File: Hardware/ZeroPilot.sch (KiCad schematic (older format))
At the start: 5 parts

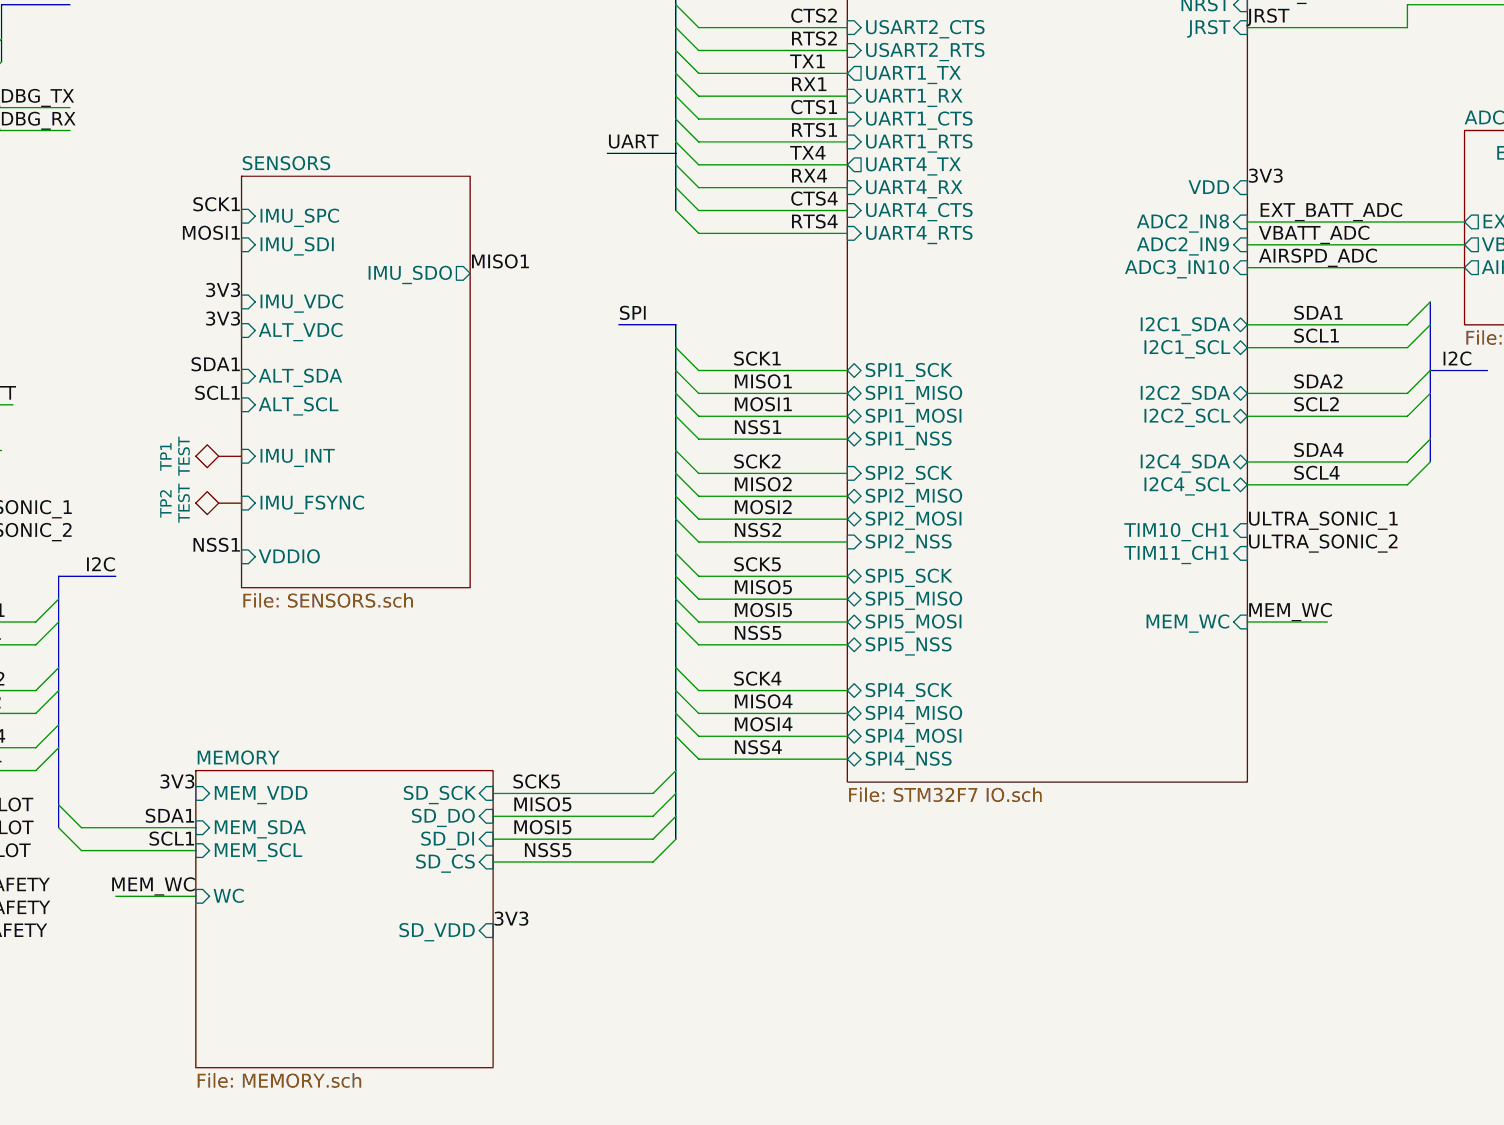
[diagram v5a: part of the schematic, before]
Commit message: Updated schematic
-Changed diode to 0603 diodes
-Changed SD card to proper pinout
-Fixed SPI1 conflict
-Renamed some power nets
-Fixed naming error in IMU NSS
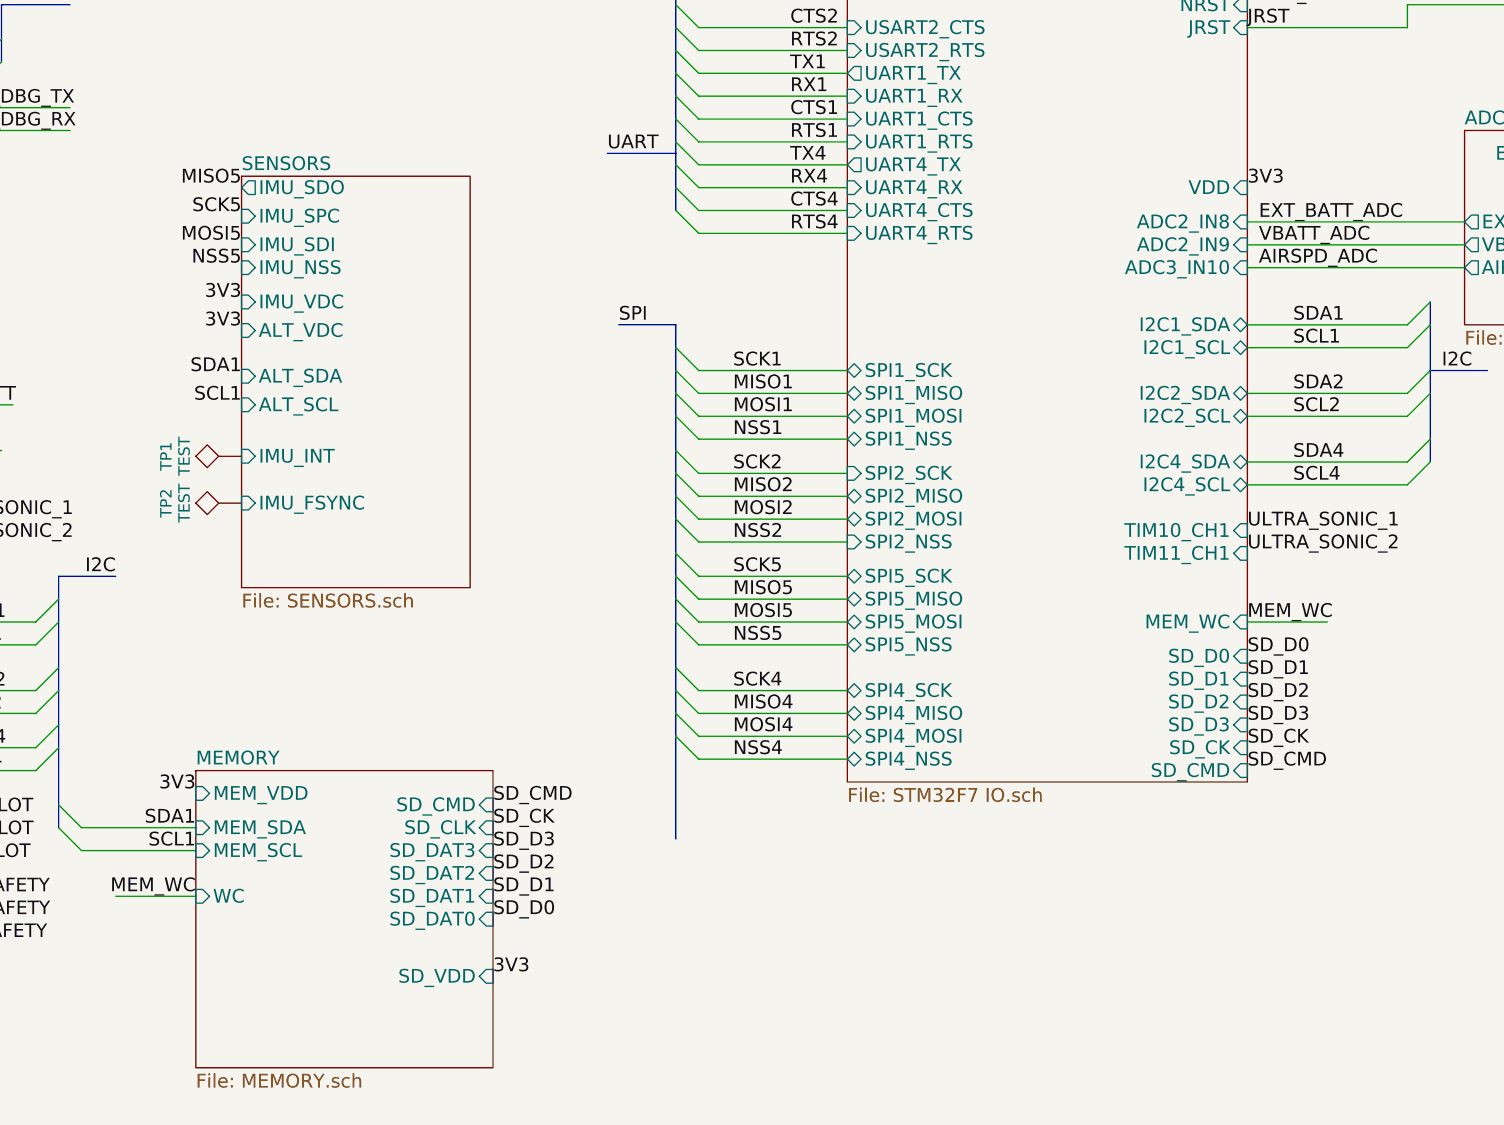
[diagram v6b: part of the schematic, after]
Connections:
- net labels added: SD_CK, SD_CMD, SD_D0, SD_D1, SD_D2, SD_D3
- wire segments 104 -> 100
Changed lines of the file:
@@
 F49 "SPI4_MOSI" B L 7200 6100 60
 F50 "MEM_WC" I R 8950 5600 60
+F51 "SD_D0" I R 8950 5750 60
+F52 "SD_D1" I R 8950 5850 60
+F53 "SD_D2" I R 8950 5950 60
+F54 "SD_D3" I R 8950 6050 60
+F55 "SD_CK" I R 8950 6150 60
+F56 "SD_CMD" I R 8950 6250 60
 $EndSheet
 Text Label 3550 850  2    60   ~ 0
@@
 F0 "MEMORY" 60
 F1 "MEMORY.sch" 60
-F2 "SD_DI" I R 5650 6550 60
-F3 "SD_DO" I R 5650 6450 60
-F4 "SD_SCK" I R 5650 6350 60
-F5 "SD_VDD" I R 5650 6950 60
-F6 "SD_CS" I R 5650 6650 60
-F7 "MEM_VDD" I L 4350 6350 60
-F8 "MEM_SDA" I L 4350 6500 60
-F9 "MEM_SCL" I L 4350 6600 60
-F10 "WC" I L 4350 6800 60
+F2 "SD_VDD" I R 5650 7150 60
+F3 "MEM_VDD" I L 4350 6350 60
+F4 "MEM_SDA" I L 4350 6500 60
+F5 "MEM_SCL" I L 4350 6600 60
+F6 "WC" I L 4350 6800 60
+F7 "SD_CMD" I R 5650 6400 60
+F8 "SD_DAT0" I R 5650 6900 60
+F9 "SD_CLK" I R 5650 6500 60
+F10 "SD_DAT3" I R 5650 6600 60
+F11 "SD_DAT1" I R 5650 6800 60
+F12 "SD_DAT2" I R 5650 6700 60
 $EndSheet
 Text Label 8950 5600 0    60   ~ 0
@@
 Text Label 4350 6350 2    60   ~ 0
 3V3
-Entry Wire Line
-	6450 6450 6350 6550
-Entry Wire Line
-	6450 6250 6350 6350
-Entry Wire Line
-	6450 6350 6350 6450
 Text Label 6200 4300 0    60   ~ 0
 SPI
@@
 NSS4
 Text Label 6700 5700 0    60   ~ 0
-NSS5
-Entry Wire Line
-	6450 6550 6350 6650
-Text Label 5950 6350 2    60   ~ 0
-SCK5
-Text Label 6000 6450 2    60   ~ 0
-MISO5
-Text Label 6000 6550 2    60   ~ 0
-MOSI5
-Text Label 6000 6650 2    60   ~ 0
 NSS5
 Text Label 9800 4500 0    60   ~ 0
@@
 	1    0    0    -1
 $EndComp
-Text Label 5650 6950 0    60   ~ 0
+Text Label 5650 7150 0    60   ~ 0
 3V3
 Text Label 3150 4500 0    60   ~ 0
@@
 F2 "IMU_SPC" I L 4550 3825 60
 F3 "IMU_SDI" I L 4550 3950 60
-F4 "IMU_SDO" O R 5550 4075 60
+F4 "IMU_SDO" O L 4550 3700 60
 F5 "ALT_SDA" I L 4550 4525 60
 F6 "ALT_SCL" I L 4550 4650 60
 F7 "IMU_VDC" I L 4550 4200 60
-F8 "VDDIO" I L 4550 5315 60
-F9 "IMU_FSYNC" I L 4550 5080 60
-F10 "ALT_VDC" I L 4550 4325 60
-F11 "IMU_INT" I L 4550 4875 60
+F8 "IMU_FSYNC" I L 4550 5080 60
+F9 "ALT_VDC" I L 4550 4325 60
+F10 "IMU_INT" I L 4550 4875 60
+F11 "IMU_NSS" I L 4550 4050 60
 $EndSheet
 Text Label 4550 3825 2    60   ~ 0
-SCK1
+SCK5
 Text Label 4550 3950 2    60   ~ 0
-MOSI1
-Text Label 5550 4075 0    60   ~ 0
-MISO1
+MOSI5
+Text Label 4550 3700 2    60   ~ 0
+MISO5
 Text Label 4550 4525 2    60   ~ 0
 SDA1
@@
 Text Label 4550 4325 2    60   ~ 0
 3V3
-Text Label 4550 5315 2    60   ~ 0
-NSS1
+Text Label 4550 4050 2    60   ~ 0
+NSS5
 Text Notes 12175 3550 0    118  ~ 24
 I2C1: altimeter
@@
 Wire Wire Line
 	4350 6800 4000 6800
-Wire Wire Line
-	6350 6350 5650 6350
-Wire Wire Line
-	5650 6450 6350 6450
-Wire Wire Line
-	6350 6550 5650 6550
 Wire Bus Line
 	6450 4300 6450 6550
@@
 Wire Wire Line
 	6550 6200 7200 6200
-Wire Wire Line
-	5650 6650 6350 6650
 Wire Bus Line
 	9750 4200 9750 4900
@@
 Text Label 8600 1950 2    60   ~ 0
 NRST_SAFETY
+Text Label 8950 5750 0    60   ~ 0
+SD_D0
+Text Label 8950 5850 0    60   ~ 0
+SD_D1
+Text Label 8950 5950 0    60   ~ 0
+SD_D2
+Text Label 8950 6050 0    60   ~ 0
+SD_D3
+Text Label 8950 6150 0    60   ~ 0
+SD_CK
+Text Label 8950 6250 0    60   ~ 0
+SD_CMD
+Text Label 5650 6900 0    60   ~ 0
+SD_D0
+Text Label 5650 6800 0    60   ~ 0
+SD_D1
+Text Label 5650 6700 0    60   ~ 0
+SD_D2
+Text Label 5650 6600 0    60   ~ 0
+SD_D3
+Text Label 5650 6500 0    60   ~ 0
+SD_CK
+Text Label 5650 6400 0    60   ~ 0
+SD_CMD
 $EndSCHEMATC

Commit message: Remapped symbols for KiCAD 5.0.x
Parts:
- TP1, TP2, TP27, TP28, TP29: symbol TEST -> Connector:TestPoint
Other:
- moved on the sheet: TP1, TP2, TP27, TP28, TP29
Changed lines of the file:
@@
-EESchema Schematic File Version 2
-LIBS:WARG
-LIBS:power
-LIBS:device
-LIBS:transistors
-LIBS:conn
-LIBS:linear
-LIBS:regul
-LIBS:74xx
-LIBS:cmos4000
-LIBS:adc-dac
-LIBS:memory
-LIBS:xilinx
-LIBS:microcontrollers
-LIBS:dsp
-LIBS:microchip
-LIBS:analog_switches
-LIBS:motorola
-LIBS:texas
-LIBS:intel
-LIBS:audio
-LIBS:interface
-LIBS:digital-audio
-LIBS:philips
-LIBS:display
-LIBS:cypress
-LIBS:siliconi
-LIBS:opto
-LIBS:atmel
-LIBS:contrib
-LIBS:valves
+EESchema Schematic File Version 4
 LIBS:ZeroPilot-cache
-EELAYER 25 0
+EELAYER 26 0
 EELAYER END
 $Descr A4 11693 8268
@@
 SCLK_SAFETY
 $Comp
-L GND #PWR01
+L power:GND #PWR01
 U 1 1 594F2D3B
 P 12300 5850
@@
 $EndComp
 $Comp
-L PWR_FLAG #FLG02
+L power:PWR_FLAG #FLG02
 U 1 1 594F3124
 P 12300 5850
@@
 I2C1: altimeter
 $Comp
-L TEST TP1
+L Connector:TestPoint TP1
 U 1 1 5B17AD8A
 P 4550 4875
@@
 $EndComp
 $Comp
-L TEST TP2
+L Connector:TestPoint TP2
 U 1 1 5B17B9D1
 P 4550 5080
@@
 	4350 6800 4000 6800
 Wire Bus Line
-	6450 4300 6450 6550
-Wire Bus Line
 	6450 4300 6200 4300
 Wire Wire Line
@@
 	6550 6200 7200 6200
 Wire Bus Line
-	9750 4200 9750 4900
-Wire Bus Line
 	9750 4500 10000 4500
 Wire Wire Line
@@
 Wire Wire Line
 	8950 4600 9650 4600
-Wire Bus Line
-	3750 5400 3750 6500
 Wire Wire Line
 	3850 6500 4350 6500
@@
 	3850 6600 4350 6600
 Wire Bus Line
-	6450 2300 6450 3800
-Wire Bus Line
 	6450 3550 6150 3550
 Wire Wire Line
@@
 Wire Wire Line
 	7200 2500 6550 2500
-Wire Bus Line
-	600  2950 600  4250
 Wire Wire Line
 	700  3150 1350 3150
@@
 	1350 4350 700  4350
 Wire Bus Line
-	3500 2900 3500 3150
-Wire Bus Line
 	3500 2900 3800 2900
 Wire Wire Line
@@
 	3150 3450 3800 3450
 Wire Bus Line
-	600  5700 600  7400
-Wire Bus Line
 	600  5700 850  5700
 Wire Wire Line
@@
 Wire Bus Line
 	5800 1200 5650 1200
-Wire Bus Line
-	5650 1200 5650 1550
 Wire Wire Line
 	5550 1350 5300 1350
@@
 Wire Bus Line
 	5800 1750 5650 1750
-Wire Bus Line
-	5650 1750 5650 1950
 Wire Wire Line
 	5550 1900 5300 1900
@@
 Wire Bus Line
 	10950 800  10700 800
-Wire Bus Line
-	10700 800  10700 1450
-Wire Bus Line
-	10700 1400 10700 1400
 Wire Wire Line
 	9850 1550 10600 1550
@@
 5V_USB
 $Comp
-L TEST TP27
+L Connector:TestPoint TP27
 U 1 1 5B375115
 P 10350 2700
@@
 $EndComp
 $Comp
-L TEST TP28
+L Connector:TestPoint TP28
 U 1 1 5B375EC5
 P 10500 2800
@@
 $EndComp
 $Comp
-L TEST TP29
+L Connector:TestPoint TP29
 U 1 1 5B37635D
 P 10600 2900
@@
 Text Label 5650 6400 0    60   ~ 0
 SD_CMD
+Wire Bus Line
+	9750 4200 9750 4500
+Wire Bus Line
+	3500 2900 3500 3150
+Wire Bus Line
+	9750 4500 9750 4900
+Wire Bus Line
+	5650 1750 5650 1950
+Wire Bus Line
+	5650 1200 5650 1550
+Wire Bus Line
+	10700 800  10700 1450
+Wire Bus Line
+	3750 5400 3750 6500
+Wire Bus Line
+	6450 2300 6450 3800
+Wire Bus Line
+	600  2950 600  4250
+Wire Bus Line
+	6450 4300 6450 6550
+Wire Bus Line
+	600  5700 600  7400
 $EndSCHEMATC
